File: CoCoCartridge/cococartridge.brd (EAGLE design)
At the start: 88.9 x 63.5 mm, 52 parts, among them IC1 LPC1769, IC2 LD1117S33, IC3 DP83848C, P1 COCO-CART3.5X2.5, Q1 BSS84, U1 USD-SOCKETNEW, X1 MINI-USB-UX60-MB-5ST

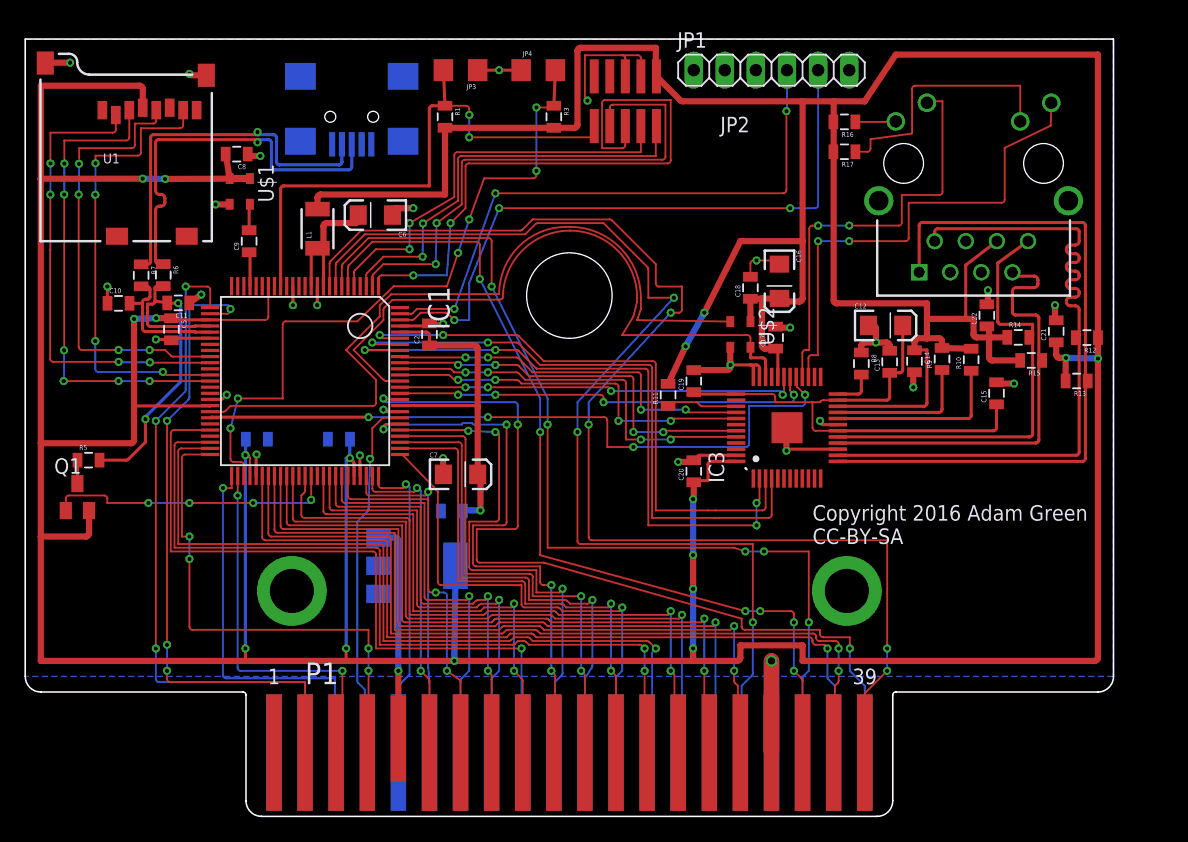
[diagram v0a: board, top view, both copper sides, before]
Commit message: Revision 1.0 sent to OSHPark
This is the first version that I sent off to OSHPark for manufacturing
tonight.
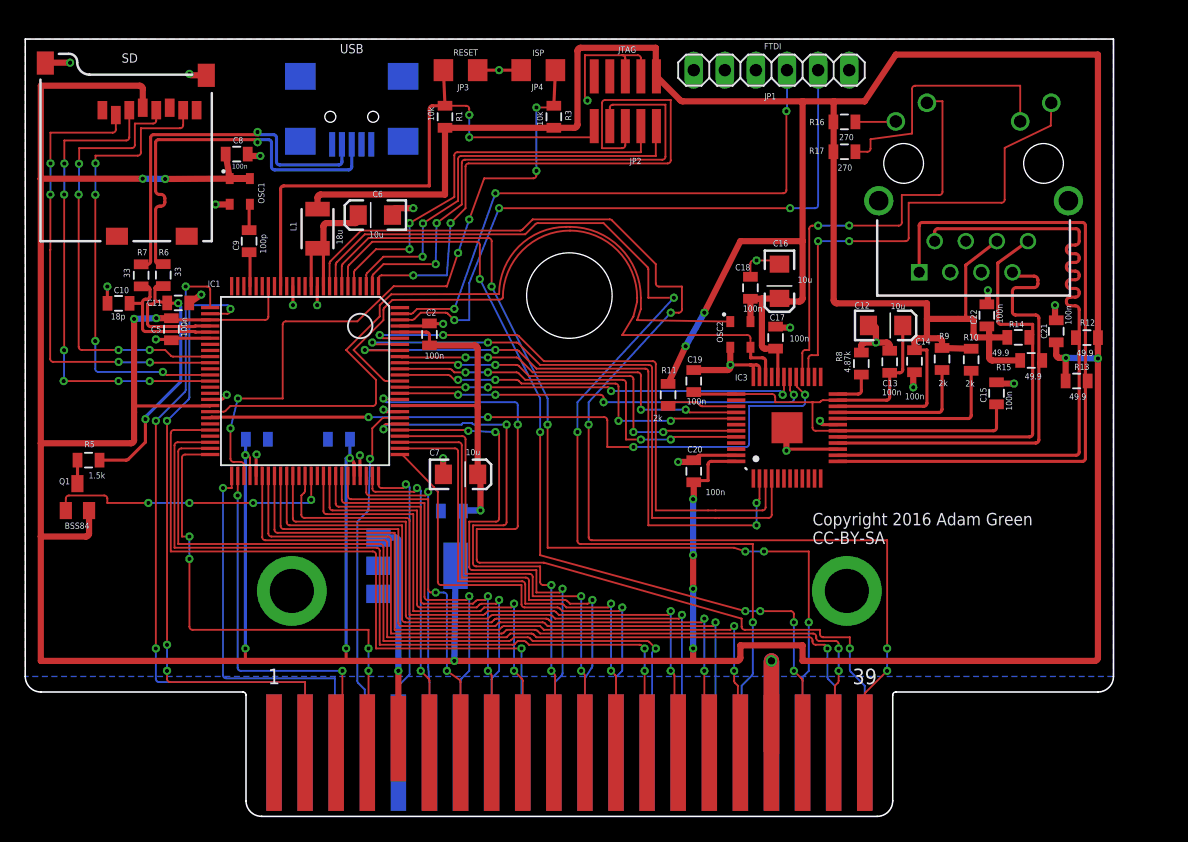
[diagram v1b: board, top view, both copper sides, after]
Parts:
- JP3: value JUMPER-1206 -> RESET
- JP4: value JUMPER-1206 -> ISP
- renumbered U$1 to OSC1, U$2 to OSC2, U1 to SD, X1 to USB

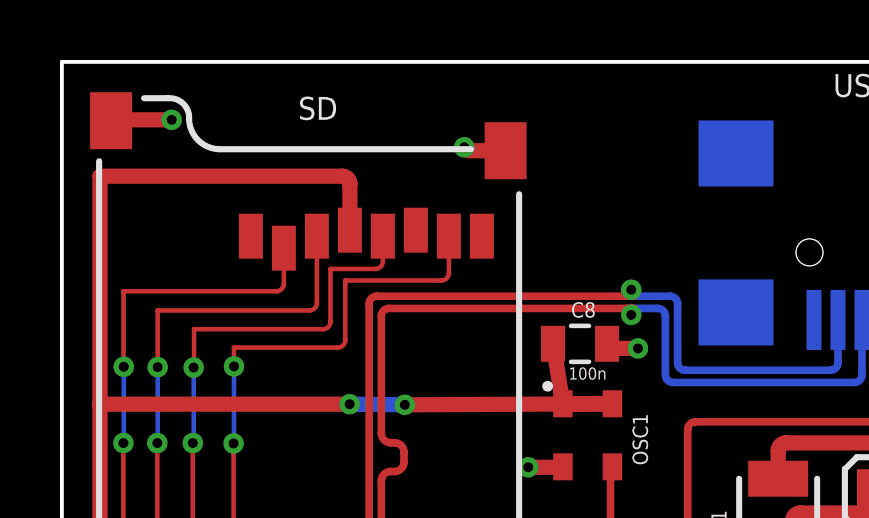
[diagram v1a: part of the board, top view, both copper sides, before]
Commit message: Fix missing Gnd connection on SD socket
I connected the shield pins labelled ground to the actual ground but
forgot to connect the actual ground pin of the SD card to my ground
plane.
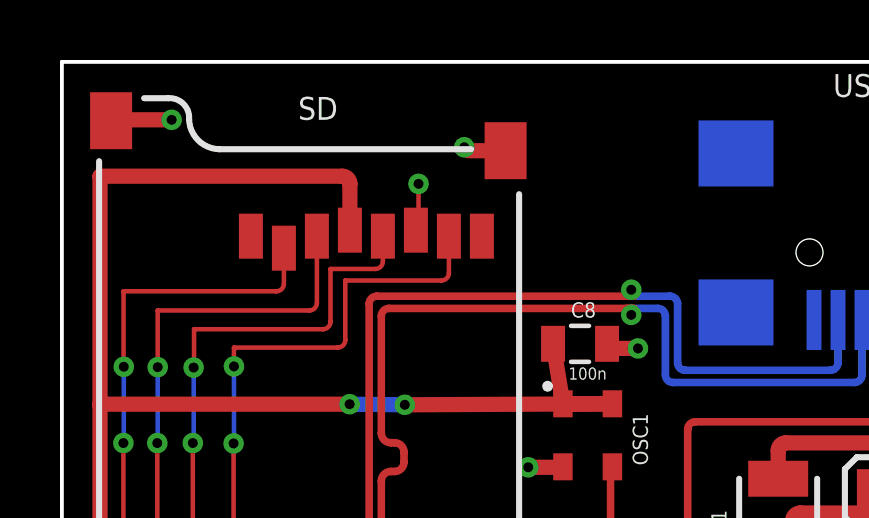
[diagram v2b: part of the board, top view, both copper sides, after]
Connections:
- net GND: now also SD.GND
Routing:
- net GND: track 96.9 -> 98.5 mm, vias 30 -> 31
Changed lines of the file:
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@@
 <wire x1="50.038" y1="62.1792" x2="48.768" y2="62.1792" width="0.1524" layer="1"/>
 <wire x1="27.36" y1="27.81" x2="27.3304" y2="29.4894" width="0.254" layer="1"/>
+<contactref element="SD" pad="GND"/>
+<via x="11.8872" y="59.436" extent="1-16" drill="0.3302"/>
+<wire x1="11.8" y1="57.89" x2="11.8872" y2="57.89" width="0.1524" layer="1"/>
+<wire x1="11.8872" y1="57.89" x2="11.8872" y2="59.436" width="0.1524" layer="1"/>
 </signal>
 </signals>
